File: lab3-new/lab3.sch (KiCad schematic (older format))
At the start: 14 parts, among them J1 Conn_01x02_Male, J2 USB_A, U1 Regulator

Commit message: Finished footprint creation and board setup
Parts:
- C1, C2: footprint (none) -> Capacitor_SMD:C_0201_0603Metric
- D1: footprint (none) -> lab3-new:led
- D2: footprint (none) -> lab3-new:diode
- F1: footprint (none) -> Fuse:Fuse_0201_0603Metric
- J1: footprint (none) -> Connector:JWT_A3963_1x02_P3.96mm_Vertical
- J2: footprint (none) -> Connector_USB:USB_A_CNCTech_1001-011-01101_Horizontal
- L1, L2: footprint (none) -> Inductor_SMD:L_6.3x6.3_H3
- R1, R2, R3, R4: footprint (none) -> Resistor_SMD:R_0201_0603Metric
- U1: footprint (none) -> lab3-new:regulator
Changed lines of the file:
@@
 F 0 "R1" H 8520 3396 50  0000 L CNN
 F 1 "120" H 8520 3305 50  0000 L CNN
-F 2 "" V 8380 3350 50  0001 C CNN
+F 2 "Resistor_SMD:R_0201_0603Metric" V 8380 3350 50  0001 C CNN
 F 3 "~" H 8450 3350 50  0001 C CNN
 	1    8450 3350
@@
 F 0 "D1" V 8489 3633 50  0000 R CNN
 F 1 "LED" V 8398 3633 50  0000 R CNN
-F 2 "" H 8450 3750 50  0001 C CNN
+F 2 "lab3-new:led" H 8450 3750 50  0001 C CNN
 F 3 "~" H 8450 3750 50  0001 C CNN
 	1    8450 3750
@@
 F 0 "R2" H 7970 3546 50  0000 L CNN
 F 1 "150" H 7970 3455 50  0000 L CNN
-F 2 "" V 7830 3500 50  0001 C CNN
+F 2 "Resistor_SMD:R_0201_0603Metric" V 7830 3500 50  0001 C CNN
 F 3 "~" H 7900 3500 50  0001 C CNN
 	1    7900 3500
@@
 F 0 "D2" H 4650 3084 50  0000 C CNN
 F 1 "D_Schottky" H 4650 3175 50  0000 C CNN
-F 2 "" H 4650 3300 50  0001 C CNN
+F 2 "lab3-new:diode" H 4650 3300 50  0001 C CNN
 F 3 "~" H 4650 3300 50  0001 C CNN
 	1    4650 3300
@@
 F 0 "U1" H 5250 3085 50  0000 C CNN
 F 1 "Regulator" H 5250 3176 50  0000 C CNN
-F 2 "" H 5250 3500 50  0001 C CNN
+F 2 "lab3-new:regulator" H 5250 3500 50  0001 C CNN
 F 3 "" H 5250 3500 50  0001 C CNN
 	1    5250 3500
@@
 F 0 "J1" H 3758 3481 50  0000 C CNN
 F 1 "Conn_01x02_Male" H 3758 3390 50  0000 C CNN
-F 2 "" H 3650 3300 50  0001 C CNN
+F 2 "Connector:JWT_A3963_1x02_P3.96mm_Vertical" H 3650 3300 50  0001 C CNN
 F 3 "~" H 3650 3300 50  0001 C CNN
 	1    3650 3300
@@
 F 0 "J2" H 7357 3917 50  0000 C CNN
 F 1 "USB_A" H 7357 3826 50  0000 C CNN
-F 2 "" H 7450 3400 50  0001 C CNN
+F 2 "Connector_USB:USB_A_CNCTech_1001-011-01101_Horizontal" H 7450 3400 50  0001 C CNN
 F 3 " ~" H 7450 3400 50  0001 C CNN
 	1    7300 3450
@@
 F 0 "F1" V 4153 3300 50  0000 C CNN
 F 1 "Fuse" V 4244 3300 50  0000 C CNN
-F 2 "" V 4280 3300 50  0001 C CNN
+F 2 "Fuse:Fuse_0201_0603Metric" V 4280 3300 50  0001 C CNN
 F 3 "~" H 4350 3300 50  0001 C CNN
 	1    4350 3300
@@
 F 0 "C1" H 6415 3496 50  0000 L CNN
 F 1 "C" H 6415 3405 50  0000 L CNN
-F 2 "" H 6338 3300 50  0001 C CNN
+F 2 "Capacitor_SMD:C_0201_0603Metric" H 6338 3300 50  0001 C CNN
 F 3 "~" H 6300 3450 50  0001 C CNN
 	1    6300 3450
@@
 F 0 "L2" H 5853 3196 50  0000 L CNN
 F 1 "L" H 5853 3105 50  0000 L CNN
-F 2 "" H 5800 3150 50  0001 C CNN
+F 2 "Inductor_SMD:L_6.3x6.3_H3" H 5800 3150 50  0001 C CNN
 F 3 "~" H 5800 3150 50  0001 C CNN
 	1    5800 3150
@@
 F 0 "C2" H 6465 2796 50  0000 L CNN
 F 1 "C" H 6465 2705 50  0000 L CNN
-F 2 "" H 6388 2600 50  0001 C CNN
+F 2 "Capacitor_SMD:C_0201_0603Metric" H 6388 2600 50  0001 C CNN
 F 3 "~" H 6350 2750 50  0001 C CNN
 	1    6350 2750
@@
 F 0 "L1" H 4853 3696 50  0000 L CNN
 F 1 "L" H 4853 3605 50  0000 L CNN
-F 2 "" H 4800 3650 50  0001 C CNN
+F 2 "Inductor_SMD:L_6.3x6.3_H3" H 4800 3650 50  0001 C CNN
 F 3 "~" H 4800 3650 50  0001 C CNN
 	1    4800 3650
@@
 F 0 "R3" V 6293 3700 50  0000 C CNN
 F 1 "R" V 6384 3700 50  0000 C CNN
-F 2 "" V 6430 3700 50  0001 C CNN
+F 2 "Resistor_SMD:R_0201_0603Metric" V 6430 3700 50  0001 C CNN
 F 3 "~" H 6500 3700 50  0001 C CNN
 	1    6500 3700
@@
 F 0 "R4" H 5970 4096 50  0000 L CNN
 F 1 "R" H 5970 4005 50  0000 L CNN
-F 2 "" V 5830 4050 50  0001 C CNN
+F 2 "Resistor_SMD:R_0201_0603Metric" V 5830 4050 50  0001 C CNN
 F 3 "~" H 5900 4050 50  0001 C CNN
 	1    5900 4050

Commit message: smd to tht
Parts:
- C1, C2: footprint Capacitor_SMD:C_0201_0603Metric -> Capacitor_THT:C_Disc_D3.0mm_W1.6mm_P2.50mm
- L1, L2: footprint Inductor_SMD:L_6.3x6.3_H3 -> Inductor_THT:L_Axial_L5.0mm_D3.6mm_P10.00mm_Horizontal_Murata_BL01RN1A2A2
- R1, R2, R3, R4: footprint Resistor_SMD:R_0201_0603Metric -> Resistor_THT:R_Axial_DIN0204_L3.6mm_D1.6mm_P1.90mm_Vertical

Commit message: Finished layout
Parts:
- F1: footprint Fuse:Fuse_0201_0603Metric -> Fuse:Fuse_BelFuse_0ZRE0005FF_L8.3mm_W3.8mm
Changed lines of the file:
@@
-EESchema Schematic File Version 5
-EELAYER 31 0
+EESchema Schematic File Version 4
+EELAYER 30 0
 EELAYER END
 $Descr A4 11693 8268
@@
 Comment3 ""
 Comment4 ""
-Comment5 ""
-Comment6 ""
-Comment7 ""
-Comment8 ""
-Comment9 ""
 $EndDescr
 Connection ~ 5900 3700
@@
 F 0 "F1" V 4153 3300 50  0000 C CNN
 F 1 "Fuse" V 4244 3300 50  0000 C CNN
-F 2 "Fuse:Fuse_0201_0603Metric" V 4280 3300 50  0001 C CNN
+F 2 "Fuse:Fuse_BelFuse_0ZRE0005FF_L8.3mm_W3.8mm" V 4280 3300 50  0001 C CNN
 F 3 "~" H 4350 3300 50  0001 C CNN
 	1    4350 3300

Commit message: changed diode footprint and assigned to schematic
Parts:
- D2: footprint lab3-new:diode -> lab3-new:diode2
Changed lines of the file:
@@
 F 0 "D2" H 4650 3084 50  0000 C CNN
 F 1 "D_Schottky" H 4650 3175 50  0000 C CNN
-F 2 "lab3-new:diode" H 4650 3300 50  0001 C CNN
+F 2 "lab3-new:diode2" H 4650 3300 50  0001 C CNN
 F 3 "~" H 4650 3300 50  0001 C CNN
 	1    4650 3300

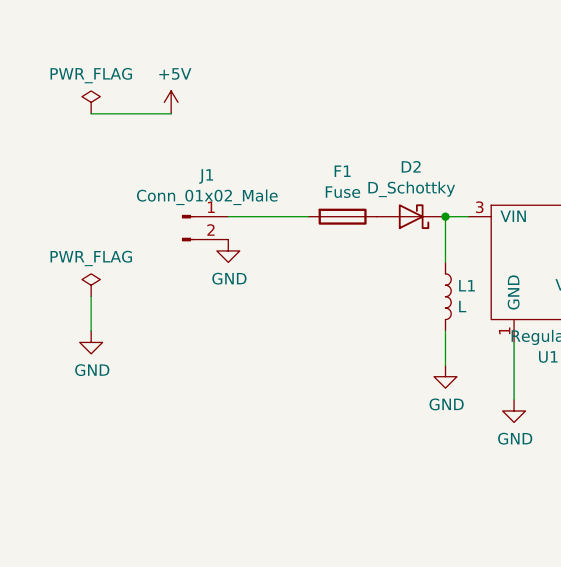
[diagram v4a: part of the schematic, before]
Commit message: updated connectors
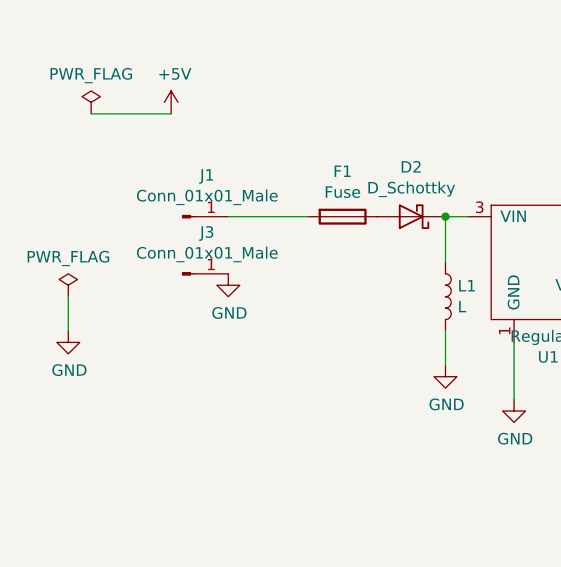
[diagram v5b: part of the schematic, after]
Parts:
- removed J1: Conn_01x02_Male, Connector:JWT_A3963_1x02_P3.96mm_Vertical, symbol Connector:Conn_01x02_Male
- added J1, J3: Conn_01x01_Male, lab3-new:connector1, symbol Connector:Conn_01x01_Male
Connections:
- net GND: now also J3.1 (Pin_1)
- net at F1.2: now also J1.1 (Pin_1)
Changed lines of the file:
@@
 	3250 2850 3600 2850
 Wire Wire Line
-	3250 3650 3250 3800
+	3150 3650 3150 3800
 Wire Wire Line
 	3850 3300 4200 3300
@@
 L power:PWR_FLAG #FLG0101
 U 1 1 5E4E97C1
-P 3250 3650
-F 0 "#FLG0101" H 3250 3725 50  0001 C CNN
-F 1 "PWR_FLAG" H 3250 3823 50  0000 C CNN
-F 2 "" H 3250 3650 50  0001 C CNN
-F 3 "~" H 3250 3650 50  0001 C CNN
-	1    3250 3650
+P 3150 3650
+F 0 "#FLG0101" H 3150 3725 50  0001 C CNN
+F 1 "PWR_FLAG" H 3150 3823 50  0000 C CNN
+F 2 "" H 3150 3650 50  0001 C CNN
+F 3 "~" H 3150 3650 50  0001 C CNN
+	1    3150 3650
 	1    0    0    -1
 $EndComp
@@
 L power:GND #PWR0101
 U 1 1 5E4EB1FC
-P 3250 3800
-F 0 "#PWR0101" H 3250 3550 50  0001 C CNN
-F 1 "GND" H 3255 3627 50  0000 C CNN
-F 2 "" H 3250 3800 50  0001 C CNN
-F 3 "" H 3250 3800 50  0001 C CNN
-	1    3250 3800
+P 3150 3800
+F 0 "#PWR0101" H 3150 3550 50  0001 C CNN
+F 1 "GND" H 3155 3627 50  0000 C CNN
+F 2 "" H 3150 3800 50  0001 C CNN
+F 3 "" H 3150 3800 50  0001 C CNN
+	1    3150 3800
 	1    0    0    -1
 $EndComp
@@
 L power:GND #PWR01
 U 1 1 5E508D65
-P 3850 3400
-F 0 "#PWR01" H 3850 3150 50  0001 C CNN
-F 1 "GND" H 3855 3227 50  0000 C CNN
-F 2 "" H 3850 3400 50  0001 C CNN
-F 3 "" H 3850 3400 50  0001 C CNN
-	1    3850 3400
+P 3850 3550
+F 0 "#PWR01" H 3850 3300 50  0001 C CNN
+F 1 "GND" H 3855 3377 50  0000 C CNN
+F 2 "" H 3850 3550 50  0001 C CNN
+F 3 "" H 3850 3550 50  0001 C CNN
+	1    3850 3550
 	1    0    0    -1
 $EndComp
@@
 $EndComp
 $Comp
-L Connector:Conn_01x02_Male J1
-U 1 1 5E507583
-P 3650 3300
-F 0 "J1" H 3758 3481 50  0000 C CNN
-F 1 "Conn_01x02_Male" H 3758 3390 50  0000 C CNN
-F 2 "Connector:JWT_A3963_1x02_P3.96mm_Vertical" H 3650 3300 50  0001 C CNN
-F 3 "~" H 3650 3300 50  0001 C CNN
-	1    3650 3300
-	1    0    0    -1
-$EndComp
-$Comp
 L Device:LED D1
 U 1 1 5E4DDF91
@@
 	1    0    0    -1
 $EndComp
+$Comp
+L Connector:Conn_01x01_Male J1
+U 1 1 5E6A0B09
+P 3650 3300
+F 0 "J1" H 3758 3481 50  0000 C CNN
+F 1 "Conn_01x01_Male" H 3758 3390 50  0000 C CNN
+F 2 "lab3-new:connector1" H 3650 3300 50  0001 C CNN
+F 3 "~" H 3650 3300 50  0001 C CNN
+	1    3650 3300
+	1    0    0    -1
+$EndComp
+$Comp
+L Connector:Conn_01x01_Male J3
+U 1 1 5E6A293F
+P 3650 3550
+F 0 "J3" H 3758 3731 50  0000 C CNN
+F 1 "Conn_01x01_Male" H 3758 3640 50  0000 C CNN
+F 2 "lab3-new:connector1" H 3650 3550 50  0001 C CNN
+F 3 "~" H 3650 3550 50  0001 C CNN
+	1    3650 3550
+	1    0    0    -1
+$EndComp
